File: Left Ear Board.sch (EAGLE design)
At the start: 5 parts

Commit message: Worked on board schematic
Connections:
- net GND: no longer U$4.P$14
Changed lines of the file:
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@@
 <part name="GND3" library="supply1" library_urn="urn:adsk.eagle:library:371" deviceset="GND" device=""/>
 <part name="GND4" library="supply1" library_urn="urn:adsk.eagle:library:371" deviceset="GND" device=""/>
-<part name="U$4" library="FormE" deviceset="QUAD_NAND" device=""/>
 <part name="P+3" library="supply1" library_urn="urn:adsk.eagle:library:371" deviceset="VCC" device=""/>
 <part name="GND5" library="supply1" library_urn="urn:adsk.eagle:library:371" deviceset="GND" device=""/>
@@
 <part name="P+4" library="supply1" library_urn="urn:adsk.eagle:library:371" deviceset="VCC" device=""/>
 <part name="GND6" library="supply1" library_urn="urn:adsk.eagle:library:371" deviceset="GND" device=""/>
+<part name="U$4" library="FormE" deviceset="QUAD_NAND" device=""/>
 </parts>
 <sheets>
@@
 <instance part="GND3" gate="1" x="187.96" y="33.02"/>
 <instance part="GND4" gate="1" x="165.1" y="96.52"/>
-<instance part="U$4" gate="G$1" x="137.16" y="-7.62" rot="R270"/>
 <instance part="P+3" gate="VCC" x="190.5" y="7.62"/>
 <instance part="GND5" gate="1" x="190.5" y="-35.56"/>
@@
 <instance part="P+4" gate="VCC" x="88.9" y="-30.48"/>
 <instance part="GND6" gate="1" x="88.9" y="-73.66"/>
+<instance part="U$4" gate="G$1" x="132.08" y="7.62" rot="R270"/>
 </instances>
 <busses>
@@
 </segment>
 <segment>
+<pinref part="SV1" gate="1" pin="8"/>
+<wire x1="86.36" y1="-45.72" x2="88.9" y2="-45.72" width="0.1524" layer="91"/>
+<wire x1="88.9" y1="-45.72" x2="88.9" y2="-33.02" width="0.1524" layer="91"/>
+<pinref part="P+4" gate="VCC" pin="VCC"/>
+</segment>
+<segment>
 <pinref part="U$4" gate="G$1" pin="P$13"/>
 <pinref part="P+3" gate="VCC" pin="VCC"/>
 <wire x1="162.56" y1="2.54" x2="190.5" y2="2.54" width="0.1524" layer="91"/>
 <wire x1="190.5" y1="2.54" x2="190.5" y2="5.08" width="0.1524" layer="91"/>
-</segment>
-<segment>
-<pinref part="SV1" gate="1" pin="8"/>
-<wire x1="86.36" y1="-45.72" x2="88.9" y2="-45.72" width="0.1524" layer="91"/>
-<wire x1="88.9" y1="-45.72" x2="88.9" y2="-33.02" width="0.1524" layer="91"/>
-<pinref part="P+4" gate="VCC" pin="VCC"/>
 </segment>
 </net>
@@
 </segment>
 <segment>
-<pinref part="U$4" gate="G$1" pin="P$14"/>
 <pinref part="GND5" gate="1" pin="GND"/>
 <wire x1="162.56" y1="-20.32" x2="190.5" y2="-20.32" width="0.1524" layer="91"/>
@@
 <segment>
 <pinref part="U$2" gate="G$1" pin="A0"/>
-<wire x1="101.6" y1="30.48" x2="101.6" y2="12.7" width="0.1524" layer="91"/>
-<wire x1="101.6" y1="12.7" x2="109.22" y2="2.54" width="0.1524" layer="91"/>
+<wire x1="101.6" y1="30.48" x2="101.6" y2="5.08" width="0.1524" layer="91"/>
 <pinref part="U$4" gate="G$1" pin="P$11"/>
+<wire x1="101.6" y1="5.08" x2="109.22" y2="5.08" width="0.1524" layer="91"/>
+<wire x1="109.22" y1="5.08" x2="109.22" y2="2.54" width="0.1524" layer="91"/>
 </segment>
 </net>
@@
 <segment>
 <pinref part="U$3" gate="G$1" pin="GS"/>
+<wire x1="167.64" y1="30.48" x2="167.64" y2="12.7" width="0.1524" layer="91"/>
 <pinref part="U$4" gate="G$1" pin="P$1"/>
-<wire x1="167.64" y1="30.48" x2="167.64" y2="12.7" width="0.1524" layer="91"/>
-<wire x1="167.64" y1="12.7" x2="152.4" y2="2.54" width="0.1524" layer="91"/>
+<wire x1="152.4" y1="2.54" x2="152.4" y2="12.7" width="0.1524" layer="91"/>
+<wire x1="152.4" y1="12.7" x2="167.64" y2="12.7" width="0.1524" layer="91"/>
 </segment>
 </net>
 <net name="2" class="0">
 <segment>
-<pinref part="U$4" gate="G$1" pin="P$6"/>
 <label x="134.62" y="-33.02" size="1.778" layer="95" rot="R90"/>
 <pinref part="SV1" gate="1" pin="5"/>
 <wire x1="86.36" y1="-53.34" x2="137.16" y2="-53.34" width="0.1524" layer="91"/>
 <wire x1="137.16" y1="-53.34" x2="137.16" y2="-20.32" width="0.1524" layer="91"/>
+<pinref part="U$4" gate="G$1" pin="P$6"/>
 </segment>
 </net>
 <net name="1" class="0">
 <segment>
-<pinref part="U$4" gate="G$1" pin="P$9"/>
 <label x="121.92" y="-33.02" size="1.778" layer="95" rot="R90"/>
 <pinref part="SV1" gate="1" pin="6"/>
 <wire x1="86.36" y1="-50.8" x2="124.46" y2="-50.8" width="0.1524" layer="91"/>
 <wire x1="124.46" y1="-50.8" x2="124.46" y2="-20.32" width="0.1524" layer="91"/>
+<pinref part="U$4" gate="G$1" pin="P$9"/>
 </segment>
 </net>
 <net name="0" class="0">
 <segment>
-<pinref part="U$4" gate="G$1" pin="P$12"/>
 <wire x1="111.76" y1="-20.32" x2="111.76" y2="-48.26" width="0.1524" layer="91"/>
 <label x="109.22" y="-33.02" size="1.778" layer="95" rot="R90"/>
 <pinref part="SV1" gate="1" pin="7"/>
 <wire x1="86.36" y1="-48.26" x2="111.76" y2="-48.26" width="0.1524" layer="91"/>
+<pinref part="U$4" gate="G$1" pin="P$12"/>
 </segment>
 </net>
 <net name="N$21" class="0">
 <segment>
-<pinref part="U$4" gate="G$1" pin="P$3"/>
 <pinref part="SV1" gate="1" pin="3"/>
 <wire x1="86.36" y1="-58.42" x2="149.86" y2="-58.42" width="0.1524" layer="91"/>
 <wire x1="149.86" y1="-58.42" x2="149.86" y2="-20.32" width="0.1524" layer="91"/>
-</segment>
-</net>
+<pinref part="U$4" gate="G$1" pin="P$3"/>
+</segment>
+</net>

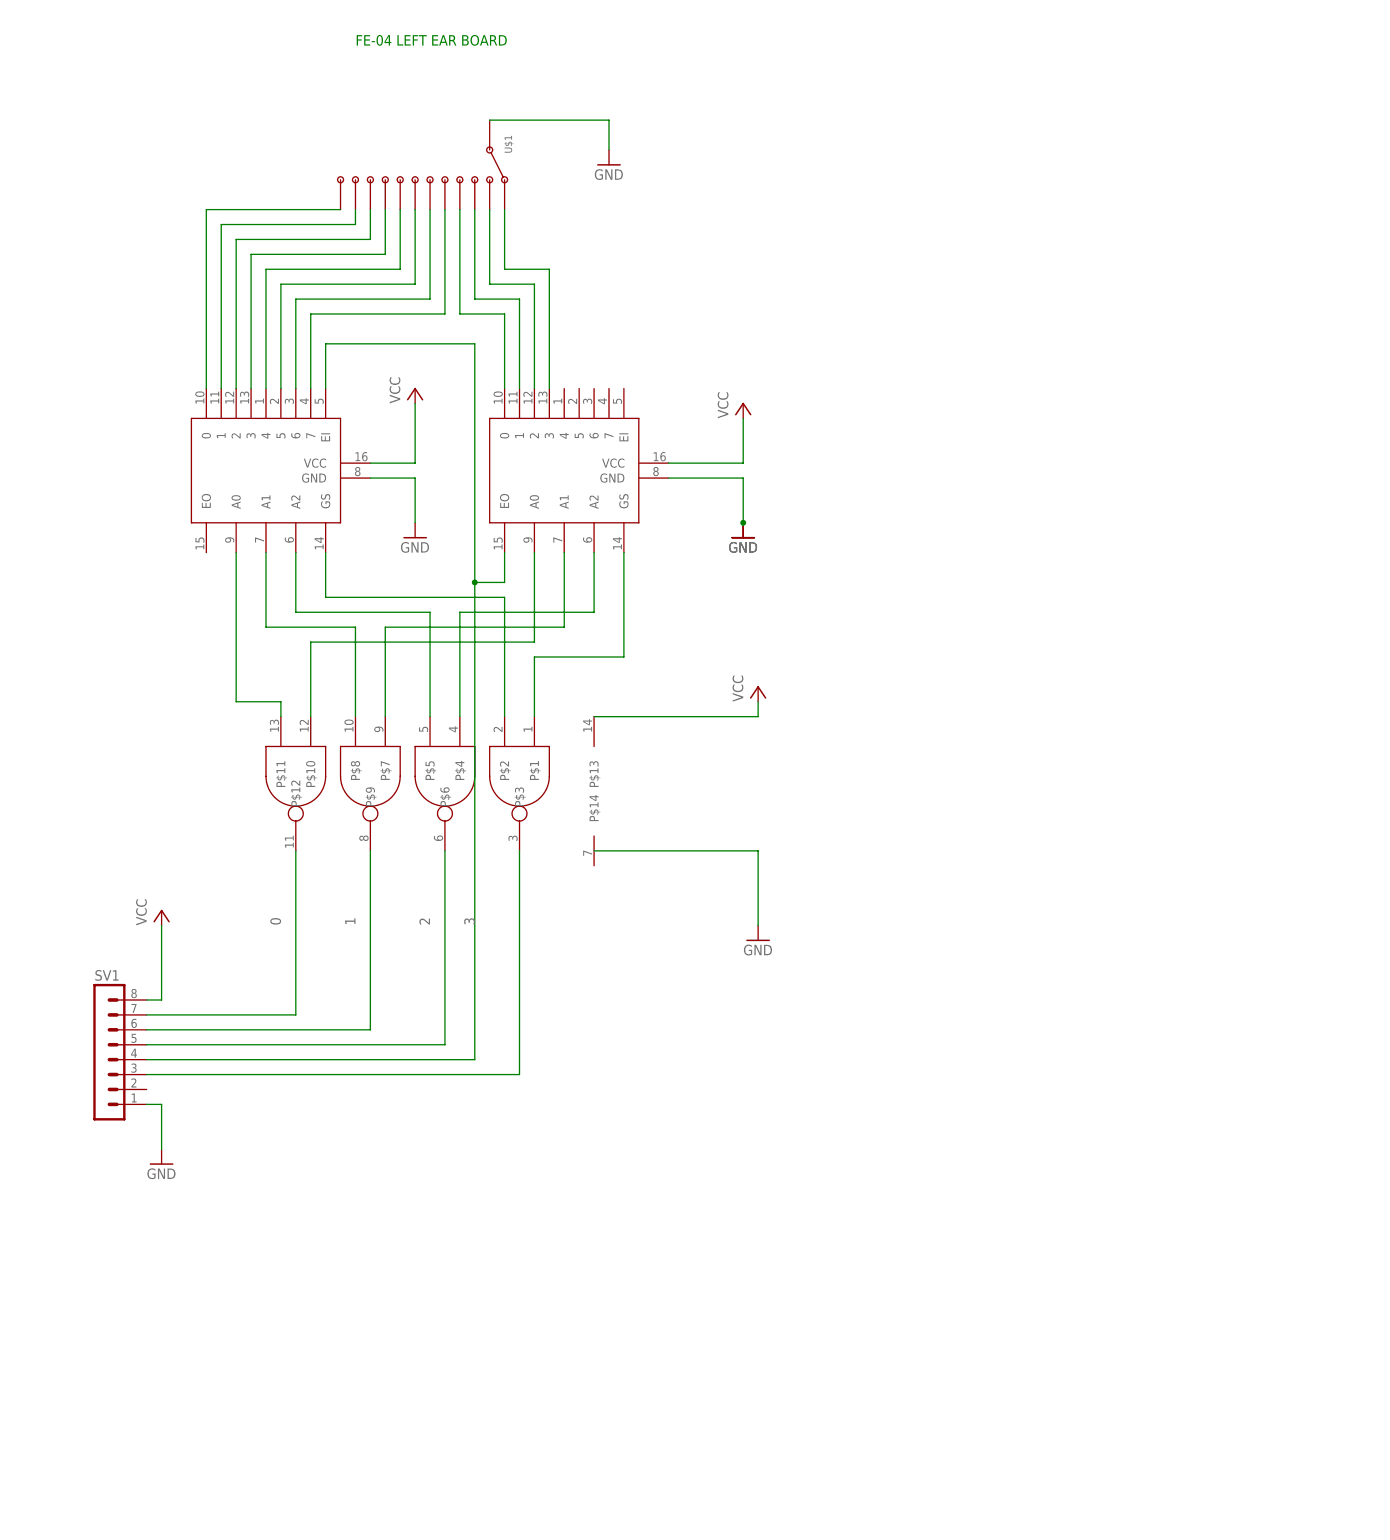
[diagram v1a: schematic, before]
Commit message: Finished Board Schematic. Routing needs to be done.
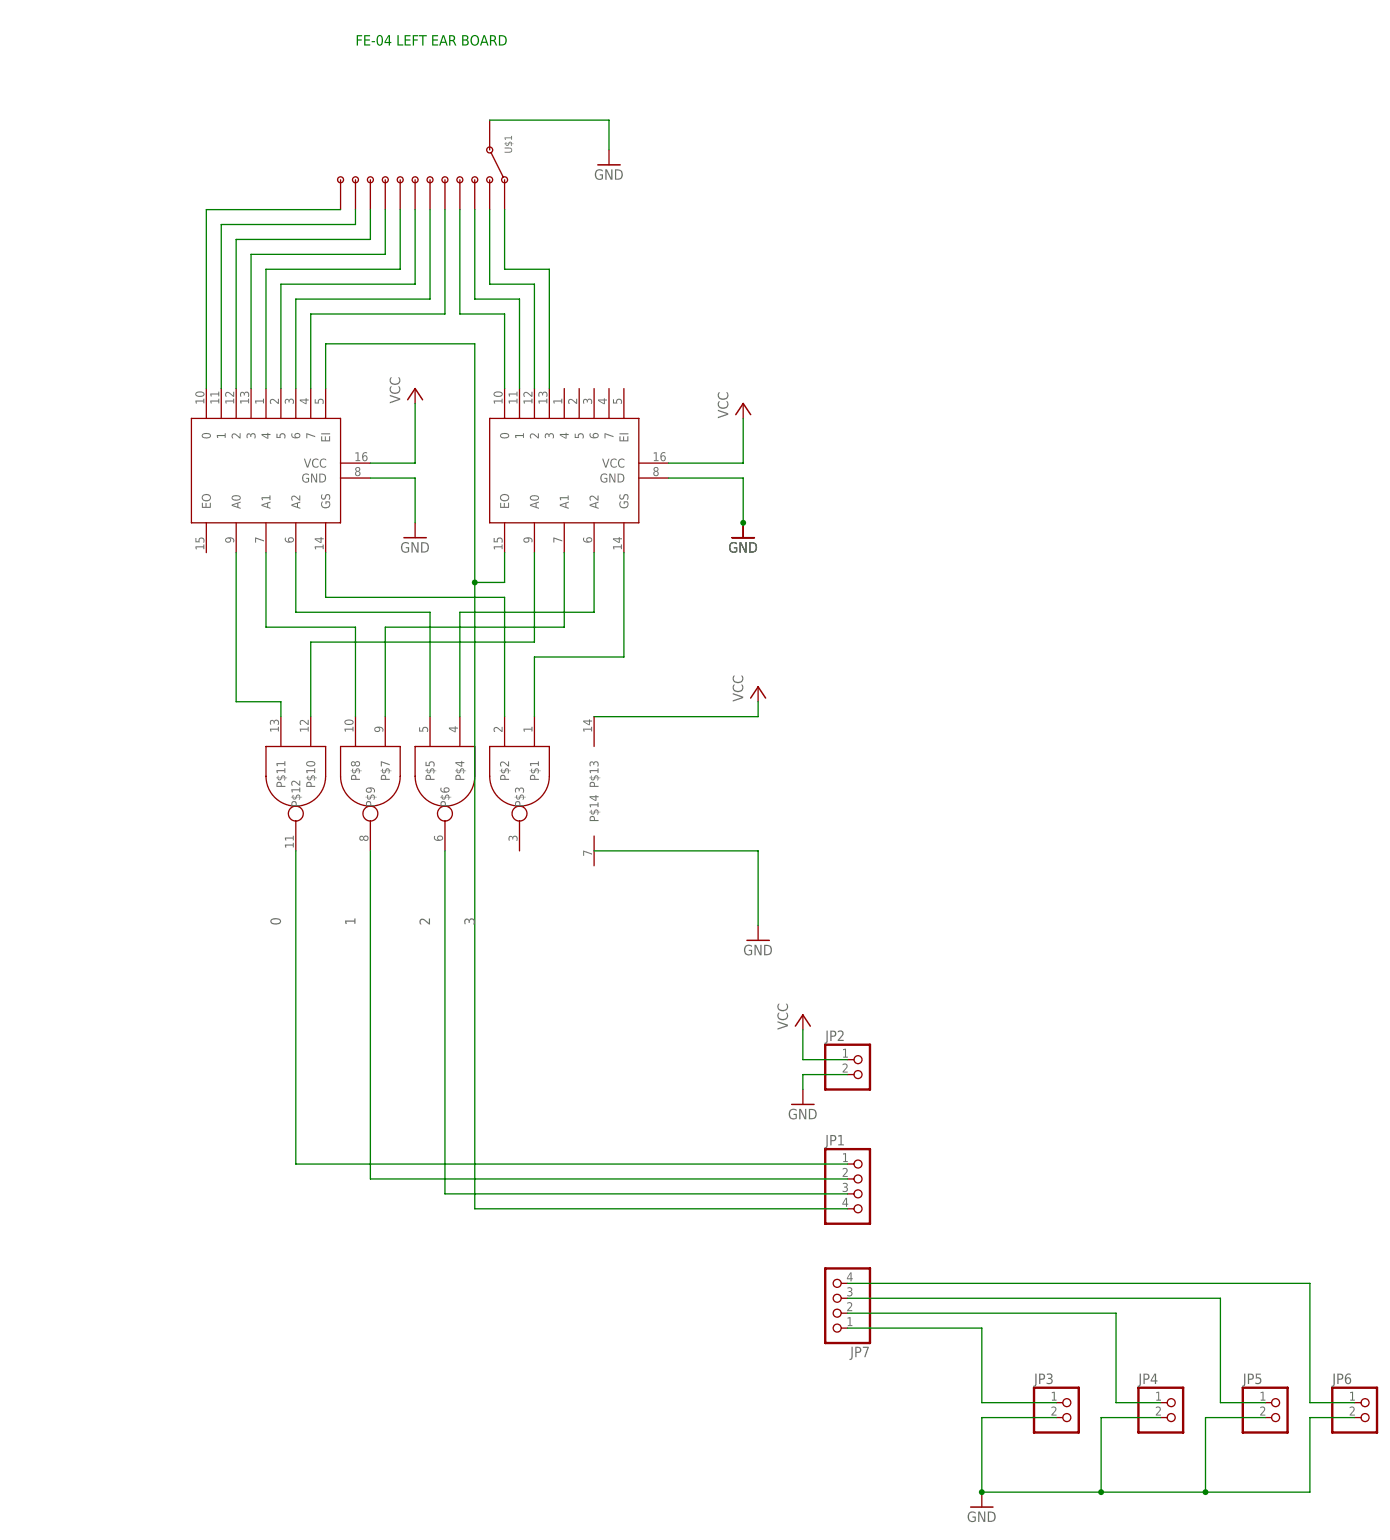
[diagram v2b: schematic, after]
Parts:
- removed SV1: (no value), con-lstb:MA08-1
- added JP1, JP7: (no value), pinhead:PINHD-1X4
- added JP2, JP3, JP4, JP5, JP6: (no value), pinhead:PINHD-1X2
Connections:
- new net N$22: JP4.1, JP7.2
- new net N$23: JP5.1, JP7.3
- new net N$24: JP6.1, JP7.4
- net 0: now also JP1.1; no longer SV1.7
- net 1: now also JP1.2; no longer SV1.6
- net 2: now also JP1.3; no longer SV1.5
- net 3: now also JP1.4; no longer SV1.4
- net GND: now also JP2.2, JP3.2, JP4.2, JP5.2, JP6.2; no longer SV1.1
- net N$21: now also JP3.1, JP7.1; no longer SV1.3, U$4.P$3
- net VCC: now also JP2.1; no longer SV1.8

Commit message: Finished board layout
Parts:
- added R1, R10, R11, R12, R2, R3, R4, R5, R6, R7, R8, R9: 10k, rcl:R-US_R0603
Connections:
- net N$1: now also R1.2
- net N$10: now also R9.1
- net N$11: now also R10.1
- net N$12: now also R11.1
- net N$13: now also R12.1
- net N$14: now also R2.2
- net N$15: now also R3.2
- net N$16: now also R4.2
- net N$17: now also R5.2
- net N$18: now also R6.2
- net N$19: now also R7.2
- net N$20: now also R8.2
- net VCC: now also R1.1, R10.2, R11.2, R12.2, R2.1, R3.1, R4.1, R5.1, R6.1, R7.1, R8.1, R9.2
